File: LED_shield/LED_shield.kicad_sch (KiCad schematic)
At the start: 8 parts, among them J101 Screw_Terminal_01x03, J102 Screw_Terminal_01x03, J103 Screw_Terminal_01x03, J104 Screw_Terminal_01x03, J105 Screw_Terminal_01x03, J106 Screw_Terminal_01x03, J107 XLR3, J108 XLR3

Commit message: Finish most of PCB design
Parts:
- added J103, J104, J105, J106, J107, J108: Screw_Terminal_01x02, Connector_Phoenix_MC:PhoenixContact_MCV_1,5_2-G-3.81_1x02_P3.81mm_Vertical, symbol Connector:Screw_Terminal_01x02
- J109: renamed from J102; footprint Connector_Phoenix_MC:PhoenixContact_MCV_1,5_3-G-3.81_1x03_P3.81mm_Vertical -> Connector_PinHeader_2.00mm:PinHeader_1x03_P2.00mm_Vertical; symbol Connector:Screw_Terminal_01x03 -> Connector:Conn_01x03_Pin
- J110: renamed from J103; footprint Connector_Phoenix_MC:PhoenixContact_MCV_1,5_3-G-3.81_1x03_P3.81mm_Vertical -> Connector_PinHeader_2.00mm:PinHeader_1x03_P2.00mm_Vertical; symbol Connector:Screw_Terminal_01x03 -> Connector:Conn_01x03_Pin
- J111: renamed from J104; footprint Connector_Phoenix_MC:PhoenixContact_MCV_1,5_3-G-3.81_1x03_P3.81mm_Vertical -> Connector_PinHeader_2.00mm:PinHeader_1x03_P2.00mm_Vertical; symbol Connector:Screw_Terminal_01x03 -> Connector:Conn_01x03_Pin
- J112: renamed from J105; footprint Connector_Phoenix_MC:PhoenixContact_MCV_1,5_3-G-3.81_1x03_P3.81mm_Vertical -> Connector_PinHeader_2.00mm:PinHeader_1x03_P2.00mm_Vertical; symbol Connector:Screw_Terminal_01x03 -> Connector:Conn_01x03_Pin
- J113: renamed from J101; footprint Connector_Phoenix_MC:PhoenixContact_MCV_1,5_3-G-3.81_1x03_P3.81mm_Vertical -> Connector_PinHeader_2.00mm:PinHeader_1x03_P2.00mm_Vertical; symbol Connector:Screw_Terminal_01x03 -> Connector:Conn_01x03_Pin
- J114: renamed from J106; footprint Connector_Phoenix_MC:PhoenixContact_MCV_1,5_3-G-3.81_1x03_P3.81mm_Vertical -> Connector_PinHeader_2.00mm:PinHeader_1x03_P2.00mm_Vertical; symbol Connector:Screw_Terminal_01x03 -> Connector:Conn_01x03_Pin
- renumbered J107 to J101, J108 to J102
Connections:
- net +5V: now also J112.1 (Pin_1), J113.1 (Pin_1), J114.1 (Pin_1), J103.1 (Pin_1), J104.1 (Pin_1), J105.1 (Pin_1)
- net +5V_{b}: now also J106.1 (Pin_1), J107.1 (Pin_1), J108.1 (Pin_1); no longer J112.1 (Pin_1), J113.1 (Pin_1), J114.1 (Pin_1)
- net GND: now also J103.2 (Pin_2), J104.2 (Pin_2), J105.2 (Pin_2), J106.2 (Pin_2), J107.2 (Pin_2), J108.2 (Pin_2)
- net IO/LED_OUT_0: now also J109.2 (Pin_2)
- net IO/LED_OUT_1: now also J110.2 (Pin_2)
- net IO/LED_OUT_2: now also J111.2 (Pin_2)
- net IO/LED_OUT_3: now also J112.2 (Pin_2)
- net IO/LED_OUT_4: now also J113.2 (Pin_2)
- net IO/LED_OUT_5: now also J114.2 (Pin_2)
- no-connect marks 0 -> 20
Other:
- sheet IO ports: added DMX_{1}R/~{W}, DMX_{2}R/~{W}; removed none
- sheet power ports: added VIN; removed none

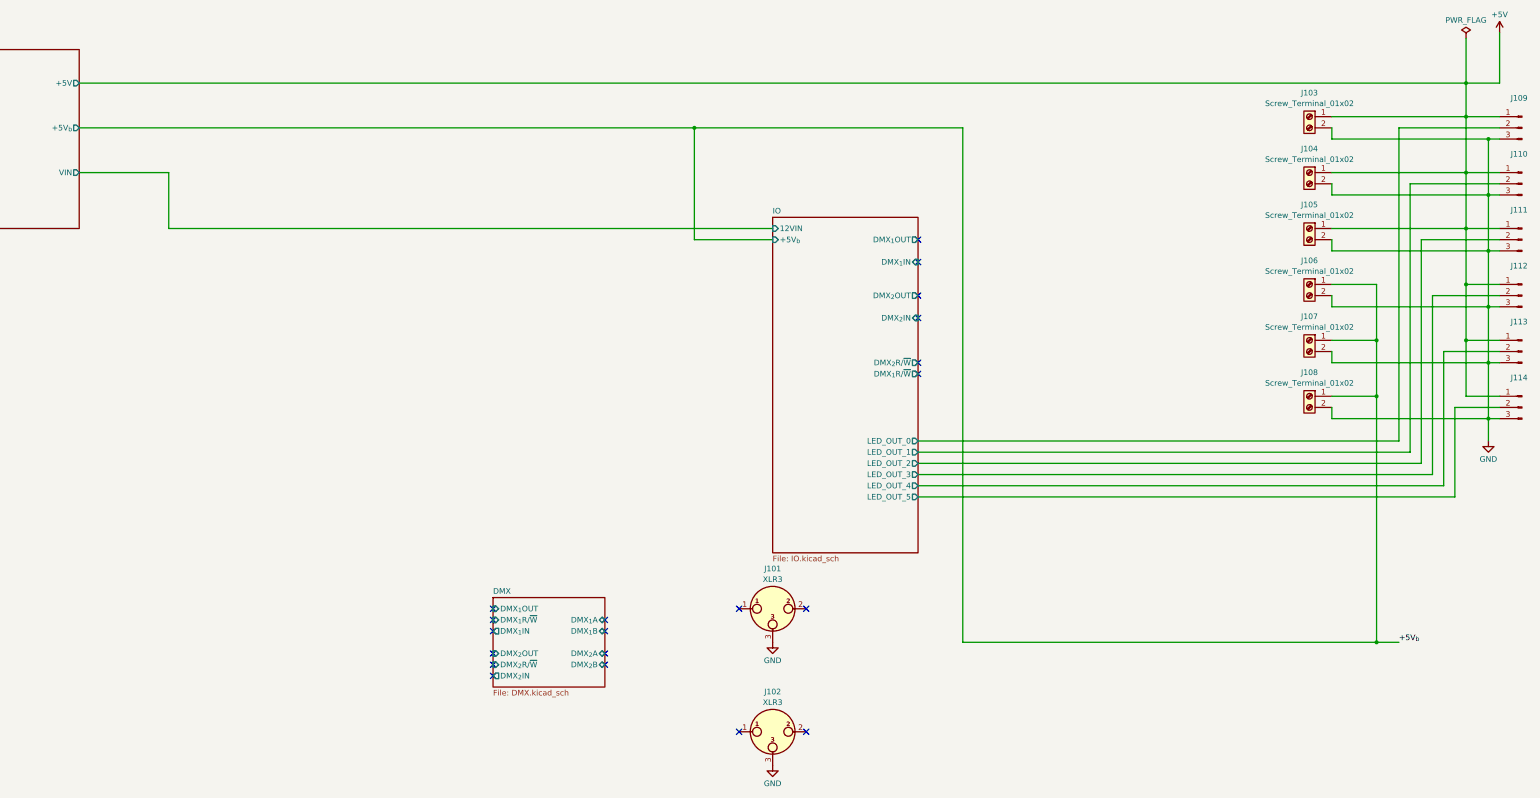
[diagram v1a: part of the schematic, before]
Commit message: Remove unused components
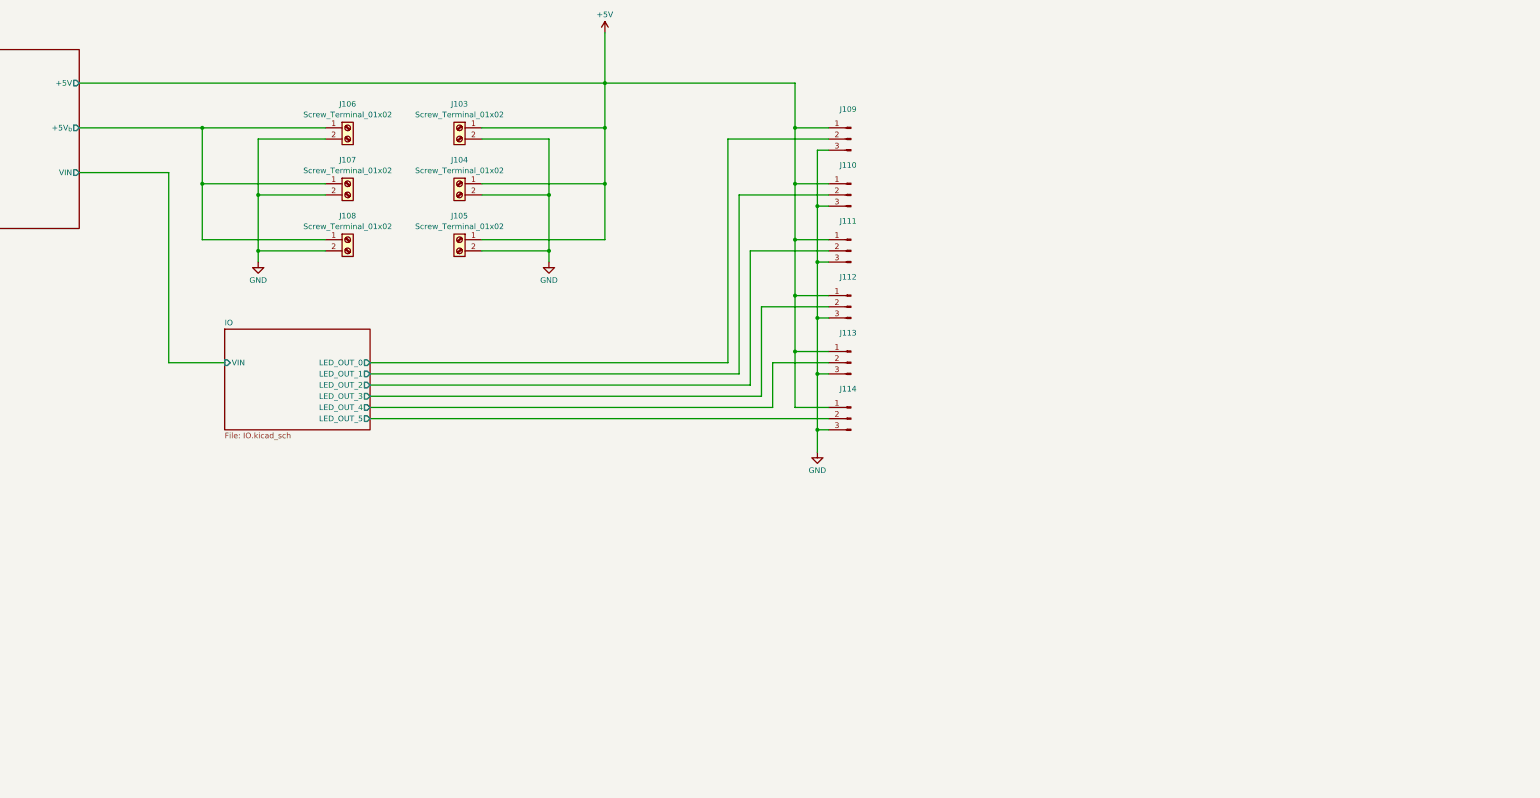
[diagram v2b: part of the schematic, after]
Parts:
- removed J101, J102: XLR3, Connector_Phoenix_MC:PhoenixContact_MCV_1,5_3-G-3.81_1x03_P3.81mm_Vertical, symbol Connector_Audio:XLR3
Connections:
- net +5V_{b} renamed power/+5V_{b}
- no-connect marks 20 -> 0
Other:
- removed sheet DMX
- sheet IO ports: added VIN; removed +5V_{b}, 12VIN, DMX_{1}IN, DMX_{1}OUT, DMX_{1}R/~{W}, DMX_{2}IN, DMX_{2}OUT, DMX_{2}R/~{W}
- moved on the sheet: J103, J104, J105, J106, J107, J108, J109, J110, J111, J112, J113, J114

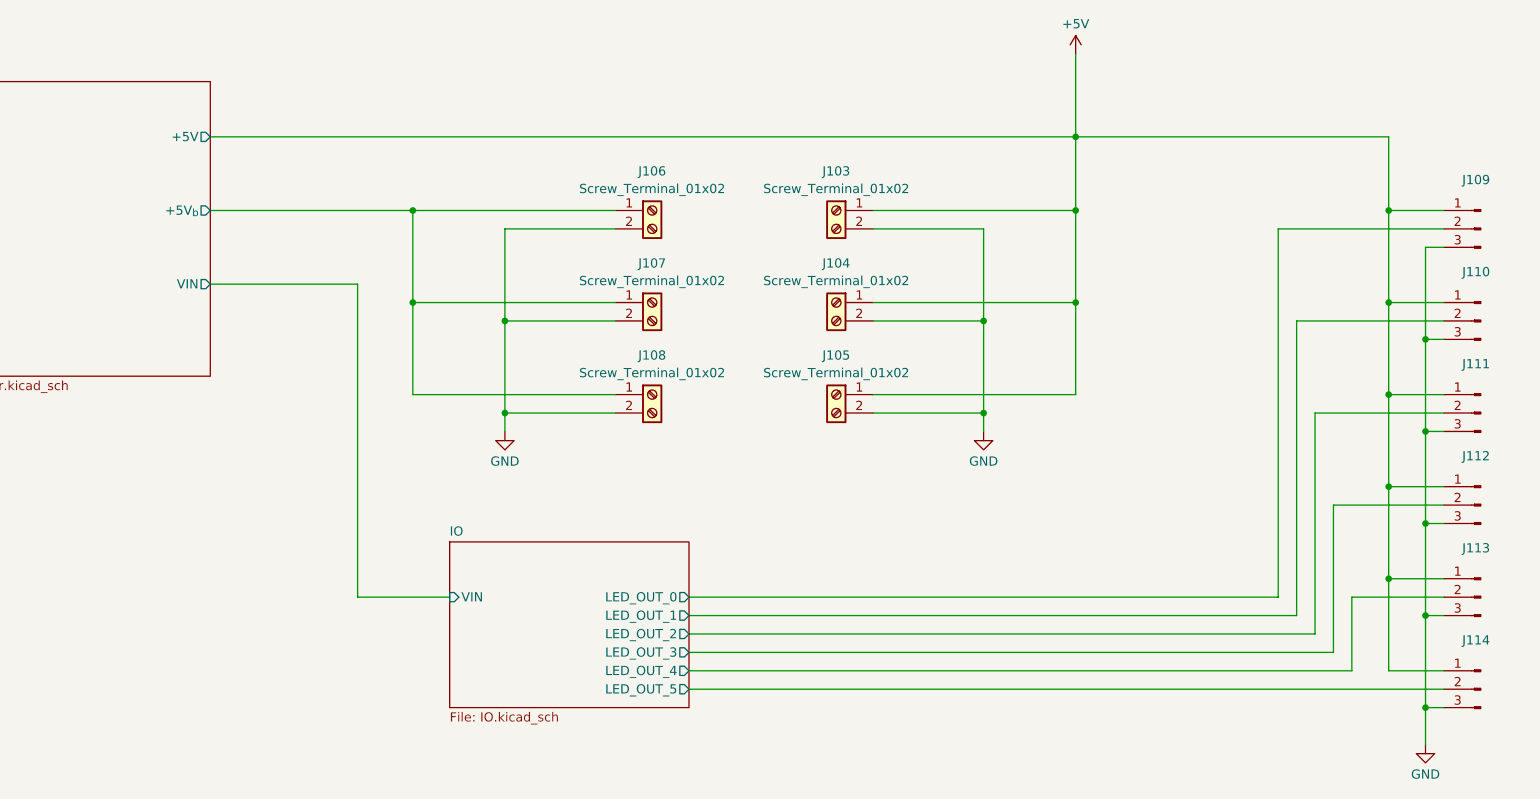
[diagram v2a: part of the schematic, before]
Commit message: Make PCB ready for manufacture (again)
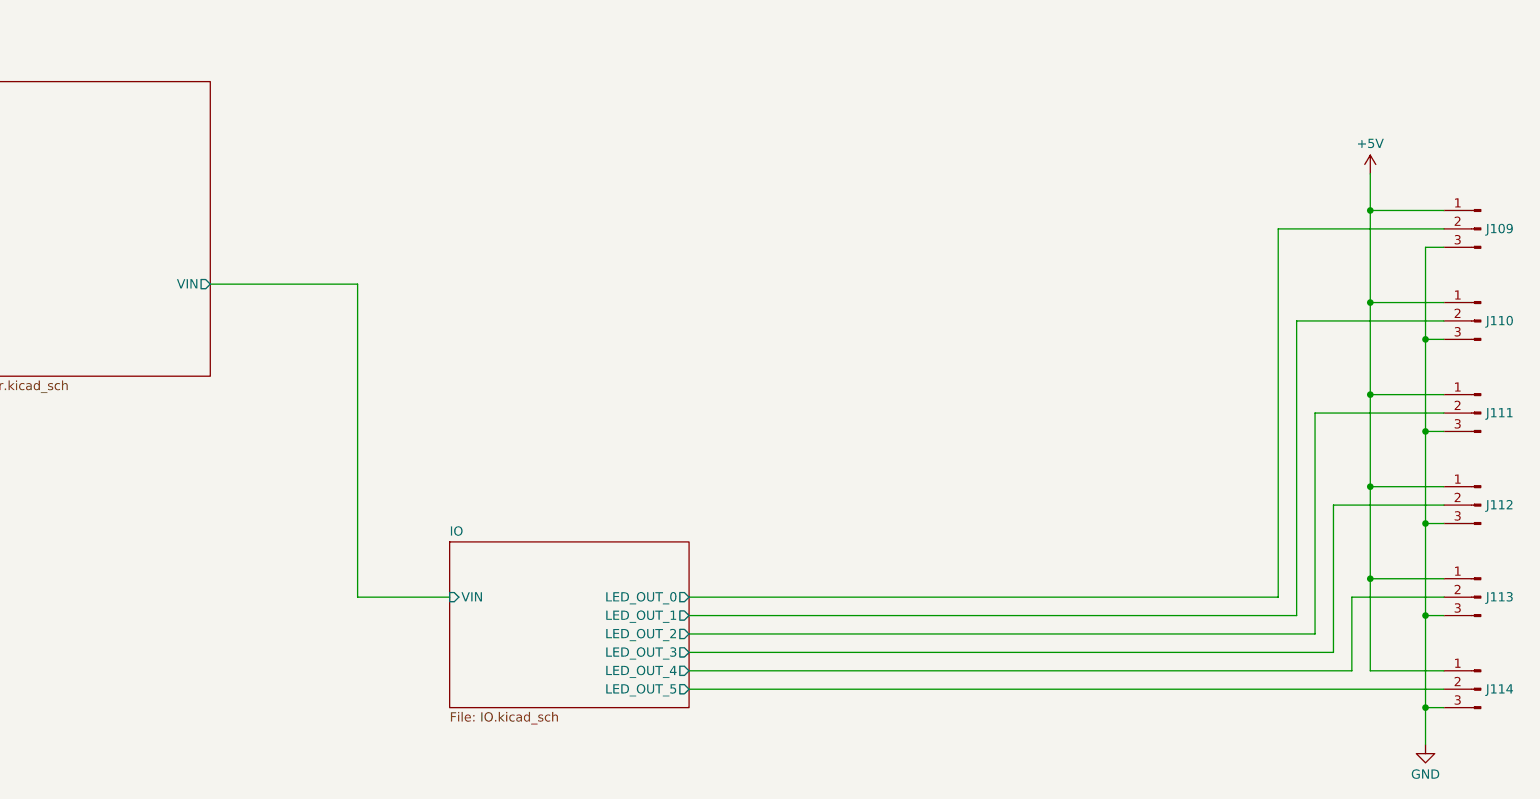
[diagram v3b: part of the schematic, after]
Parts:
- removed J103, J104, J105, J106, J107, J108: Screw_Terminal_01x02, Connector_Phoenix_MC:PhoenixContact_MCV_1,5_2-G-3.81_1x02_P3.81mm_Vertical, symbol Connector:Screw_Terminal_01x02
- J109, J110, J111, J112, J113, J114: footprint Connector_PinHeader_2.00mm:PinHeader_1x03_P2.00mm_Vertical -> Connector_PinHeader_1.00mm:PinHeader_1x03_P1.00mm_Vertical
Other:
- sheet power ports: added none; removed +5V, +5V_{b}

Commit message: Remove temp files and sync project
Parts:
- J109, J110, J111, J112, J113, J114: footprint Connector_PinHeader_1.00mm:PinHeader_1x03_P1.00mm_Vertical -> Connector_PinHeader_2.54mm:PinHeader_1x03_P2.54mm_Vertical
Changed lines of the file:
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@@
 			)
 		)
-		(property "Footprint" "Connector_PinHeader_1.00mm:PinHeader_1x03_P1.00mm_Vertical"
+		(property "Footprint" "Connector_PinHeader_2.54mm:PinHeader_1x03_P2.54mm_Vertical"
 			(at 233.68 129.54 0)
 			(effects
@@
 			)
 		)
-		(property "Footprint" "Connector_PinHeader_1.00mm:PinHeader_1x03_P1.00mm_Vertical"
+		(property "Footprint" "Connector_PinHeader_2.54mm:PinHeader_1x03_P2.54mm_Vertical"
 			(at 233.68 104.14 0)
 			(effects
@@
 			)
 		)
-		(property "Footprint" "Connector_PinHeader_1.00mm:PinHeader_1x03_P1.00mm_Vertical"
+		(property "Footprint" "Connector_PinHeader_2.54mm:PinHeader_1x03_P2.54mm_Vertical"
 			(at 233.68 91.44 0)
 			(effects
@@
 			)
 		)
-		(property "Footprint" "Connector_PinHeader_1.00mm:PinHeader_1x03_P1.00mm_Vertical"
+		(property "Footprint" "Connector_PinHeader_2.54mm:PinHeader_1x03_P2.54mm_Vertical"
 			(at 233.68 116.84 0)
 			(effects
@@
 			)
 		)
-		(property "Footprint" "Connector_PinHeader_1.00mm:PinHeader_1x03_P1.00mm_Vertical"
+		(property "Footprint" "Connector_PinHeader_2.54mm:PinHeader_1x03_P2.54mm_Vertical"
 			(at 233.68 142.24 0)
 			(effects
@@
 			)
 		)
-		(property "Footprint" "Connector_PinHeader_1.00mm:PinHeader_1x03_P1.00mm_Vertical"
+		(property "Footprint" "Connector_PinHeader_2.54mm:PinHeader_1x03_P2.54mm_Vertical"
 			(at 233.68 78.74 0)
 			(effects
